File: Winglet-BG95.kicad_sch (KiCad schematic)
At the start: 2 parts, among them M1 Mount_M2.5, M2 Mount_M2.5

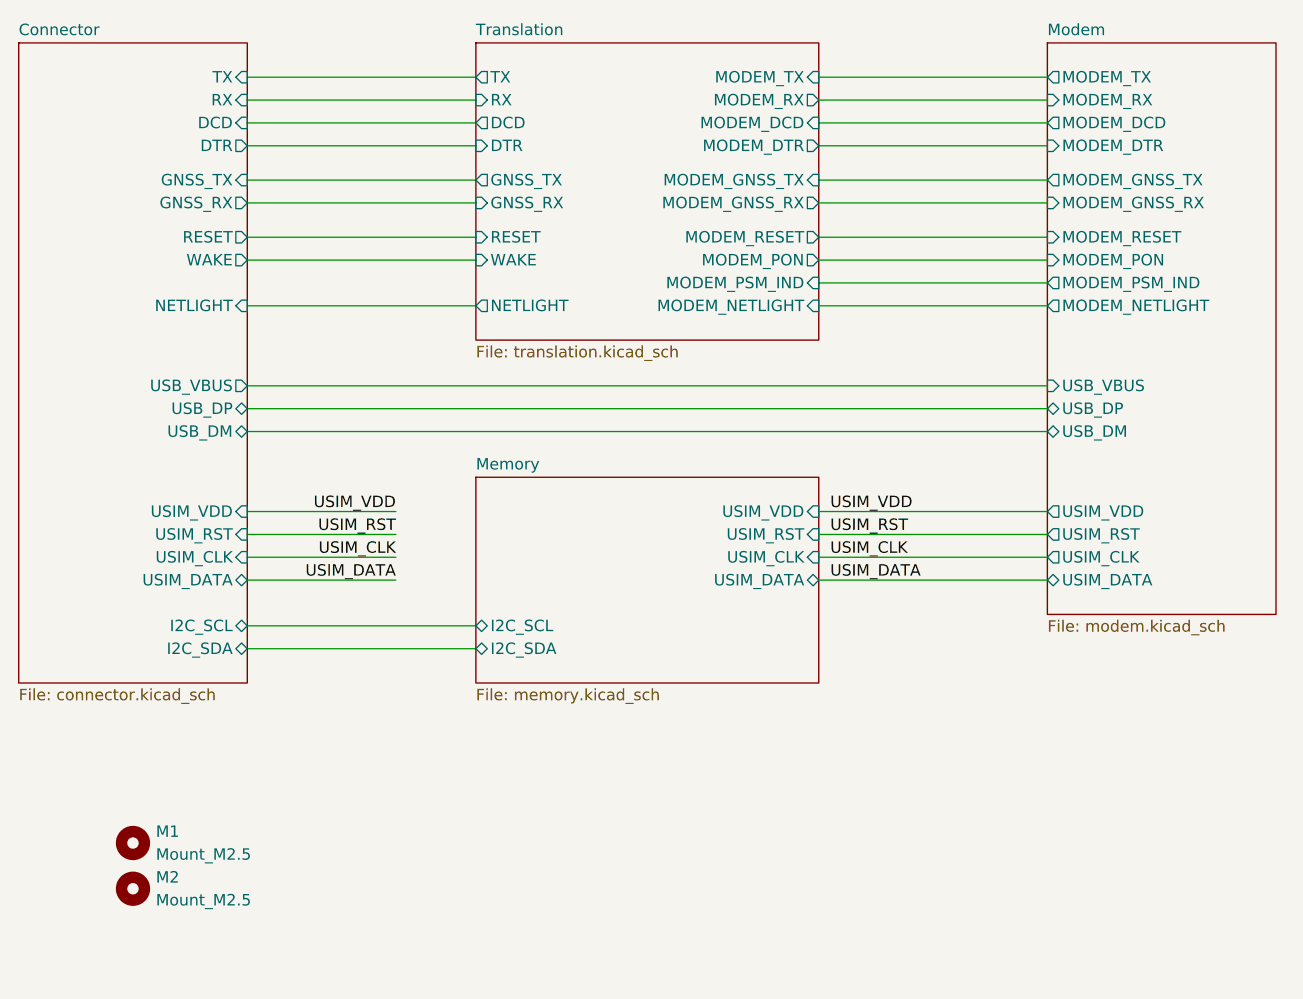
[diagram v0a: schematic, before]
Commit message: Remove PON_TRIG key, add PWRKEY control.
Remove USIM options on PCIE interface.
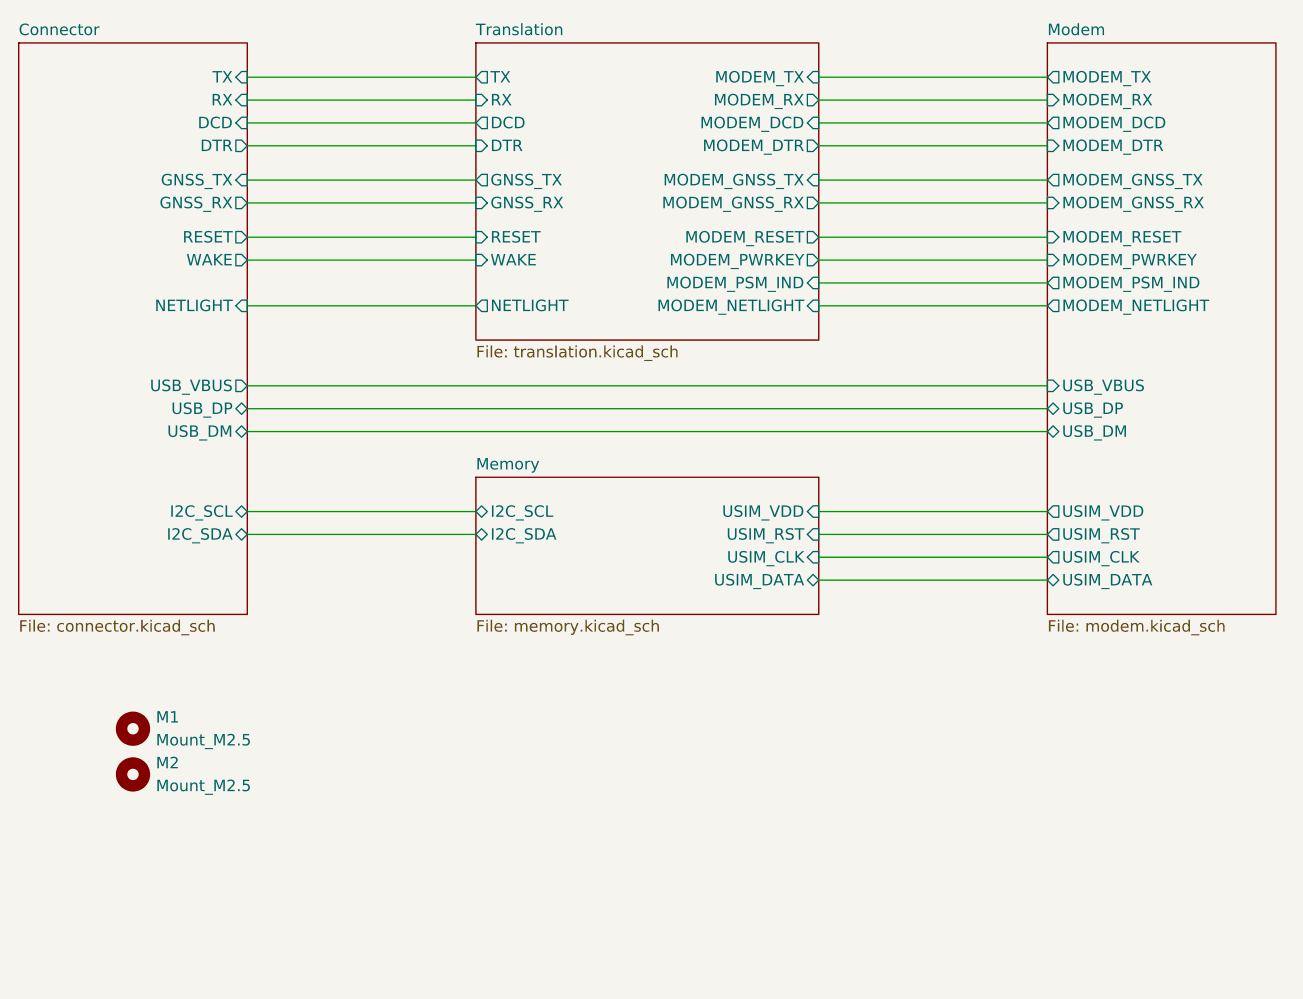
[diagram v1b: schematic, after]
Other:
- sheet Connector ports: added none; removed USIM_CLK, USIM_DATA, USIM_RST, USIM_VDD
- sheet Modem ports: added MODEM_PWRKEY; removed MODEM_PON
- sheet Translation ports: added MODEM_PWRKEY; removed MODEM_PON
- moved on the sheet: M1, M2
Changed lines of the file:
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@@
     (stroke (width 0) (type default))
   )
-  (wire (pts (xy 63.5 102.87) (xy 88.9 102.87))
+  (wire (pts (xy 63.5 90.17) (xy 88.9 90.17))
     (stroke (width 0) (type default))
   )
@@
     (stroke (width 0) (type default))
   )
-  (wire (pts (xy 63.5 105.41) (xy 88.9 105.41))
+  (wire (pts (xy 63.5 92.71) (xy 88.9 92.71))
     (stroke (width 0) (type default))
   )
@@
     (stroke (width 0) (type default))
   )
-  (wire (pts (xy 63.5 95.25) (xy 80.01 95.25))
-    (stroke (width 0) (type default))
-  )
   (wire (pts (xy 127 46.99) (xy 152.4 46.99))
     (stroke (width 0) (type default))
@@
     (stroke (width 0) (type default))
   )
-  (wire (pts (xy 63.5 97.79) (xy 80.01 97.79))
-    (stroke (width 0) (type default))
-  )
   (wire (pts (xy 127 95.25) (xy 152.4 95.25))
     (stroke (width 0) (type default))
@@
     (stroke (width 0) (type default))
   )
-  (wire (pts (xy 63.5 90.17) (xy 80.01 90.17))
-    (stroke (width 0) (type default))
-  )
-  (wire (pts (xy 63.5 92.71) (xy 80.01 92.71))
-    (stroke (width 0) (type default))
-  )
   (wire (pts (xy 127 97.79) (xy 152.4 97.79))
     (stroke (width 0) (type default))
@@
     (stroke (width 0) (type default))
   )
-  (label "USIM_CLK" (at 128.27 95.25 0) (fields_autoplaced)
-    (effects (font (size 1.27 1.27)) (justify left bottom))
-  )
-  (label "USIM_VDD" (at 128.27 90.17 0) (fields_autoplaced)
-    (effects (font (size 1.27 1.27)) (justify left bottom))
-  )
-  (label "USIM_CLK" (at 80.01 95.25 180) (fields_autoplaced)
-    (effects (font (size 1.27 1.27)) (justify right bottom))
-  )
-  (label "USIM_RST" (at 128.27 92.71 0) (fields_autoplaced)
-    (effects (font (size 1.27 1.27)) (justify left bottom))
-  )
-  (label "USIM_DATA" (at 128.27 97.79 0) (fields_autoplaced)
-    (effects (font (size 1.27 1.27)) (justify left bottom))
-  )
-  (label "USIM_VDD" (at 80.01 90.17 180) (fields_autoplaced)
-    (effects (font (size 1.27 1.27)) (justify right bottom))
-  )
-  (label "USIM_DATA" (at 80.01 97.79 180) (fields_autoplaced)
-    (effects (font (size 1.27 1.27)) (justify right bottom))
-  )
-  (label "USIM_RST" (at 80.01 92.71 180) (fields_autoplaced)
-    (effects (font (size 1.27 1.27)) (justify right bottom))
-  )
-  (symbol (lib_id "M_Mechanical:Mount_M2.5") (at 50.8 132.08 0) (unit 1)
+  (symbol (lib_id "M_Mechanical:Mount_M2.5") (at 50.8 119.38 0) (unit 1)
     (in_bom no) (on_board yes) (dnp no) (fields_autoplaced)
-    (property "Reference" "M2" (at 53.34 130.81 0)
-      (effects (font (size 1.27 1.27)) (justify left))
-    )
-    (property "Value" "Mount_M2.5" (at 53.34 133.35 0)
-      (effects (font (size 1.27 1.27)) (justify left))
-    )
-    (property "Footprint" "M_Mechanical:Mount_M2.5" (at 50.8 138.43 0)
+    (property "Reference" "M2" (at 53.34 118.11 0)
+      (effects (font (size 1.27 1.27)) (justify left))
+    )
+    (property "Value" "Mount_M2.5" (at 53.34 120.65 0)
+      (effects (font (size 1.27 1.27)) (justify left))
+    )
+    (property "Footprint" "M_Mechanical:Mount_M2.5" (at 50.8 125.73 0)
       (effects (font (size 1.27 1.27)) hide)
     )
-    (property "Datasheet" "" (at 30.48 137.16 0)
+    (property "Datasheet" "" (at 30.48 124.46 0)
       (effects (font (size 1.27 1.27)) hide)
     )
@@
     )
   )
-  (symbol (lib_id "M_Mechanical:Mount_M2.5") (at 50.8 127 0) (unit 1)
+  (symbol (lib_id "M_Mechanical:Mount_M2.5") (at 50.8 114.3 0) (unit 1)
     (in_bom no) (on_board yes) (dnp no) (fields_autoplaced)
-    (property "Reference" "M1" (at 53.34 125.73 0)
-      (effects (font (size 1.27 1.27)) (justify left))
-    )
-    (property "Value" "Mount_M2.5" (at 53.34 128.27 0)
-      (effects (font (size 1.27 1.27)) (justify left))
-    )
-    (property "Footprint" "M_Mechanical:Mount_M2.5" (at 50.8 133.35 0)
+    (property "Reference" "M1" (at 53.34 113.03 0)
+      (effects (font (size 1.27 1.27)) (justify left))
+    )
+    (property "Value" "Mount_M2.5" (at 53.34 115.57 0)
+      (effects (font (size 1.27 1.27)) (justify left))
+    )
+    (property "Footprint" "M_Mechanical:Mount_M2.5" (at 50.8 120.65 0)
       (effects (font (size 1.27 1.27)) hide)
     )
-    (property "Datasheet" "" (at 30.48 132.08 0)
+    (property "Datasheet" "" (at 30.48 119.38 0)
       (effects (font (size 1.27 1.27)) hide)
     )
@@
     )
   )
-  (sheet (at 38.1 38.1) (size 25.4 71.12) (fields_autoplaced)
+  (sheet (at 38.1 38.1) (size 25.4 63.5) (fields_autoplaced)
     (stroke (width 0.1524) (type solid))
     (fill (color 175 255 191 1.0000))
@@
       (effects (font (size 1.27 1.27)) (justify left bottom))
     )
-    (property "Sheetfile" "connector.kicad_sch" (at 38.1 109.8046 0)
+    (property "Sheetfile" "connector.kicad_sch" (at 38.1 102.1846 0)
       (effects (font (size 1.27 1.27)) (justify left top))
     )
@@
       (effects (font (size 1.27 1.27)) (justify right))
     )
-    (pin "USIM_CLK" input (at 63.5 95.25 0)
-      (effects (font (size 1.27 1.27)) (justify right))
-    )
-    (pin "USIM_RST" input (at 63.5 92.71 0)
-      (effects (font (size 1.27 1.27)) (justify right))
-    )
-    (pin "USIM_VDD" input (at 63.5 90.17 0)
-      (effects (font (size 1.27 1.27)) (justify right))
-    )
-    (pin "USIM_DATA" bidirectional (at 63.5 97.79 0)
-      (effects (font (size 1.27 1.27)) (justify right))
-    )
     (pin "RX" input (at 63.5 44.45 0)
       (effects (font (size 1.27 1.27)) (justify right))
@@
       (effects (font (size 1.27 1.27)) (justify right))
     )
-    (pin "I2C_SCL" bidirectional (at 63.5 102.87 0)
-      (effects (font (size 1.27 1.27)) (justify right))
-    )
-    (pin "I2C_SDA" bidirectional (at 63.5 105.41 0)
+    (pin "I2C_SCL" bidirectional (at 63.5 90.17 0)
+      (effects (font (size 1.27 1.27)) (justify right))
+    )
+    (pin "I2C_SDA" bidirectional (at 63.5 92.71 0)
       (effects (font (size 1.27 1.27)) (justify right))
     )
@@
       (effects (font (size 1.27 1.27)) (justify right))
     )
-    (pin "MODEM_PON" output (at 127 62.23 0)
-      (effects (font (size 1.27 1.27)) (justify right))
-    )
     (pin "MODEM_RX" output (at 127 44.45 0)
       (effects (font (size 1.27 1.27)) (justify right))
@@
     )
     (pin "MODEM_GNSS_TX" input (at 127 53.34 0)
+      (effects (font (size 1.27 1.27)) (justify right))
+    )
+    (pin "MODEM_PWRKEY" output (at 127 62.23 0)
       (effects (font (size 1.27 1.27)) (justify right))
     )
@@
       (effects (font (size 1.27 1.27)) (justify left top))
     )
-    (pin "MODEM_PON" input (at 152.4 62.23 180)
-      (effects (font (size 1.27 1.27)) (justify left))
-    )
     (pin "USB_DM" bidirectional (at 152.4 81.28 180)
       (effects (font (size 1.27 1.27)) (justify left))
@@
       (effects (font (size 1.27 1.27)) (justify left))
     )
+    (pin "MODEM_PWRKEY" input (at 152.4 62.23 180)
+      (effects (font (size 1.27 1.27)) (justify left))
+    )
     (instances
       (project "Winglet-BG95"
@@
     )
   )
-  (sheet (at 88.9 86.36) (size 38.1 22.86) (fields_autoplaced)
+  (sheet (at 88.9 86.36) (size 38.1 15.24) (fields_autoplaced)
     (stroke (width 0.1524) (type solid))
     (fill (color 175 255 191 1.0000))
@@
       (effects (font (size 1.27 1.27)) (justify left bottom))
     )
-    (property "Sheetfile" "memory.kicad_sch" (at 88.9 109.8046 0)
+    (property "Sheetfile" "memory.kicad_sch" (at 88.9 102.1846 0)
       (effects (font (size 1.27 1.27)) (justify left top))
     )
@@
       (effects (font (size 1.27 1.27)) (justify right))
     )
-    (pin "I2C_SDA" bidirectional (at 88.9 105.41 180)
-      (effects (font (size 1.27 1.27)) (justify left))
-    )
-    (pin "I2C_SCL" bidirectional (at 88.9 102.87 180)
-      (effects (font (size 1.27 1.27)) (justify left))
-    )
+    (pin "I2C_SDA" bidirectional (at 88.9 92.71 180)
+      (effects (font (size 1.27 1.27)) (justify left))
+    )
+    (pin "I2C_SCL" bidirectional (at 88.9 90.17 180)
+      (effects (font (size 1.27 1.27)) (justify left))
+    )

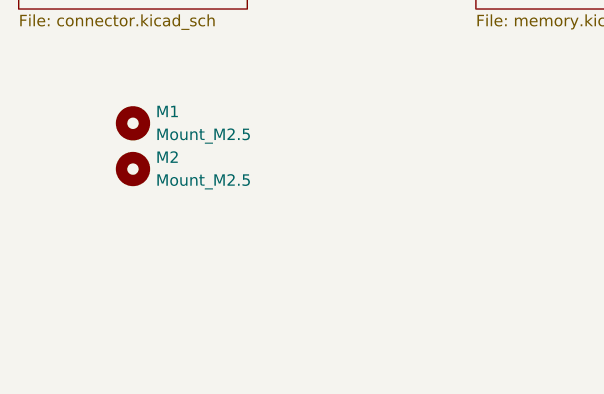
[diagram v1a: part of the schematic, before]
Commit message: Added tooling holes
Updated the readme
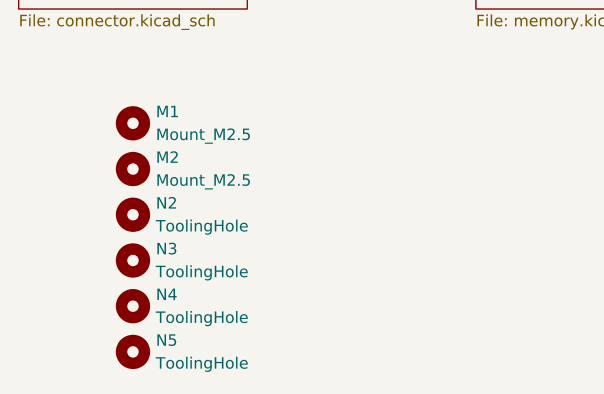
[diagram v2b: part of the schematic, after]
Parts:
- added N2, N3, N4, N5: ToolingHole, N_NonPart:ToolingHole_1mm, symbol N_NonPart:ToolingHole_1mm
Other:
- company: (none) -> TL Embedded
- title: (none) -> Winglet BG95

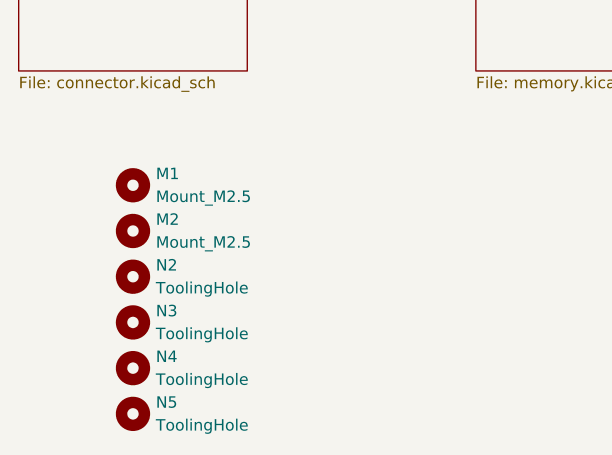
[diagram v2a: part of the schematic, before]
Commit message: Implement fixes
Closes #2
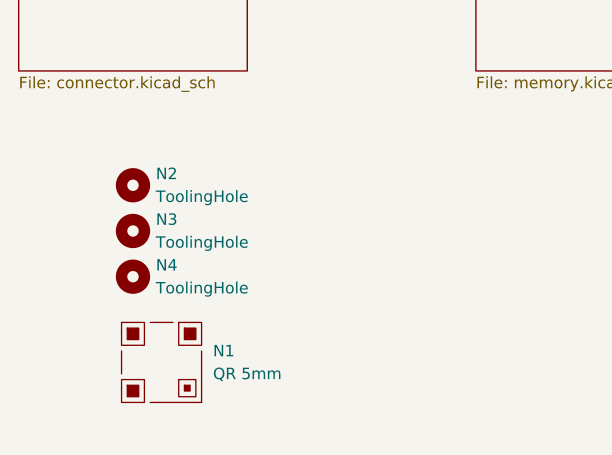
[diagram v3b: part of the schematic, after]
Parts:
- removed M1, M2: Mount_M2.5, M_Mechanical:Mount_M2.5, symbol M_Mechanical:Mount_M2.5
- removed N5: ToolingHole, N_NonPart:ToolingHole_1mm, symbol N_NonPart:ToolingHole_1mm
- added N1: QR 5mm, N_NonPart:QR_5mm_JLC, symbol N_NonPart:QR_5mm_JLC
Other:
- moved on the sheet: N2, N3, N4
